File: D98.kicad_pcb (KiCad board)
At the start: 2 copper layers, 40 x 60 mm, 44 parts, among them J1 Conn_01x08, J2 Conn_01x06, J3 Conn_01x06, J4 Conn_01x06, J5 Conn_01x05, J6 Conn_01x04, J7 Conn_01x02, J8 Conn_01x04, U1 YAAJ_BluePill_SWD_Breakout, U2 Poka Yoke

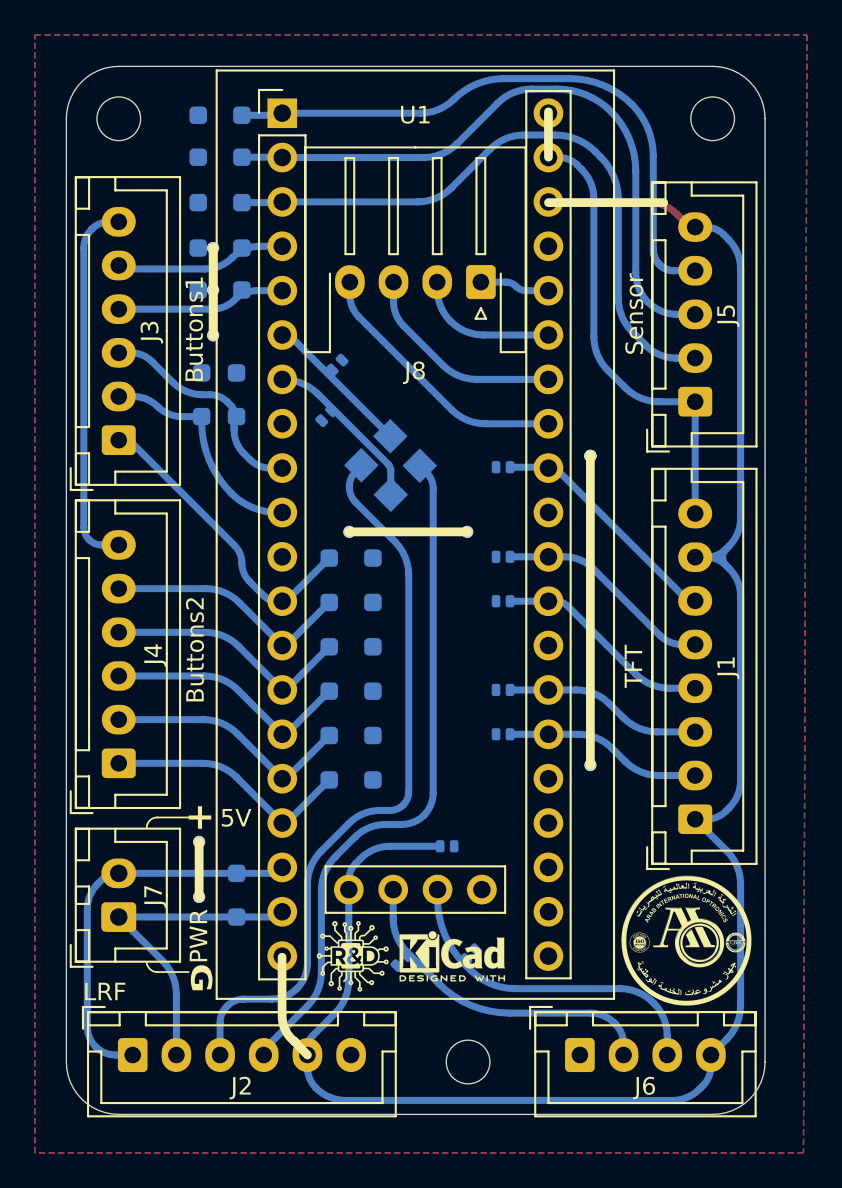
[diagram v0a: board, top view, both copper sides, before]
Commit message: Fix: Changing the EN pin of TFT from always full Brightness to becontrolled Via PWM Pin.
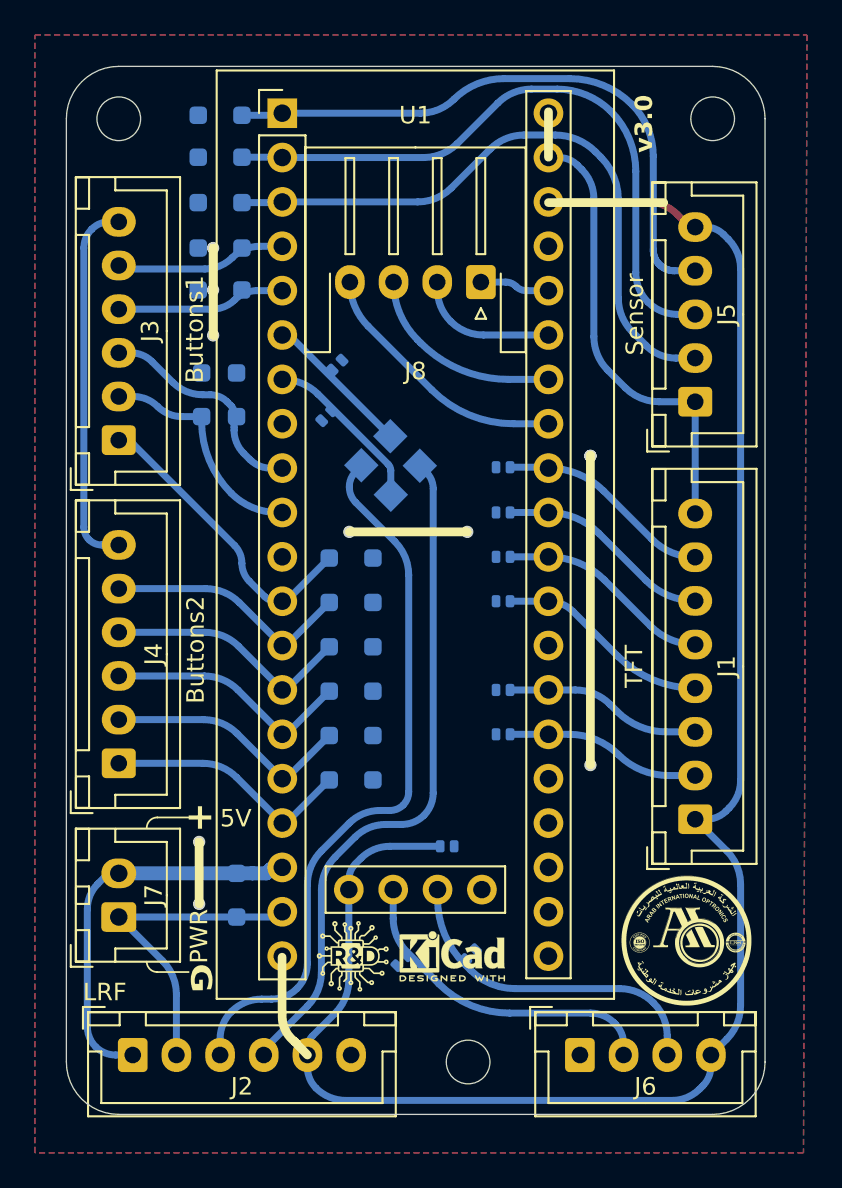
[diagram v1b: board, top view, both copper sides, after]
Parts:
- added D10: LESD8D3.3N3T5G, Diode_SMD:D_SOD-882D, B.Cu at (150.4, 95.9)
- renumbered D10 to D11, D11 to D12, D12 to D13, D13 to D14, D14 to D15, D15 to D16, D16 to D17, D17 to D18, D18 to D19, D19 to D20, D20 to D21, D21 to D22, D22 to D23, D23 to D24, D24 to D25
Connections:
- D25 pad 1: En-3.3v -> 3.3V
- J1 pad 1: En-3.3v -> 3.3V
- J1 pad 6: MOSI-A7 -> En-A6
- J1 pad 7: En-3.3v -> MOSI-A7
- J2 pad 5: En-3.3v -> 3.3V
- J5 pad 5: En-3.3v -> 3.3V
- J6 pad 4: En-3.3v -> 3.3V
- U1 pad 20: En-3.3v -> 3.3V
- U1 pad 31: unconnected-(U1-PA6-Pad31) -> En-A6
- U1 pad 38: En-3.3v -> 3.3V
- U1 pad 44: En-3.3v -> 3.3V
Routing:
- net En-3.3v: track 113.9 -> 0.00 mm
- net 3.3V: track 0.00 -> 110.2 mm
- net En-A6: track 0.00 -> 12.3 mm
- net MOSI-A7: track 13.7 -> 13.0 mm
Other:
- board text added: "${REVISION}"
- board text added: "EN"
- board text added: "EN - A6"

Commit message: fix: changed the EN pin GPIO agian from A6 to A3 because A6 is MSIO.
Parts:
- moved D4 7.62 mm to (150.4, 103.6)
- renumbered D9 to D10, D10 to D4, D4 to D5, D5 to D6, D6 to D7, D7 to D8, D8 to D9
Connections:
- D4 pad 1: En-A6 -> En-A3
- J1 pad 6: En-A6 -> En-A3
- U1 pad 28: unconnected-(U1-PA3-Pad28) -> En-A3
- U1 pad 31: En-A6 -> unconnected-(U1-PA6-Pad31)
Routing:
- net En-A3: track 0.00 -> 20.3 mm
- net En-A6: track 12.3 -> 0.00 mm
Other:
- board text added: "EN - A3"
- board text removed: "EN - A6"

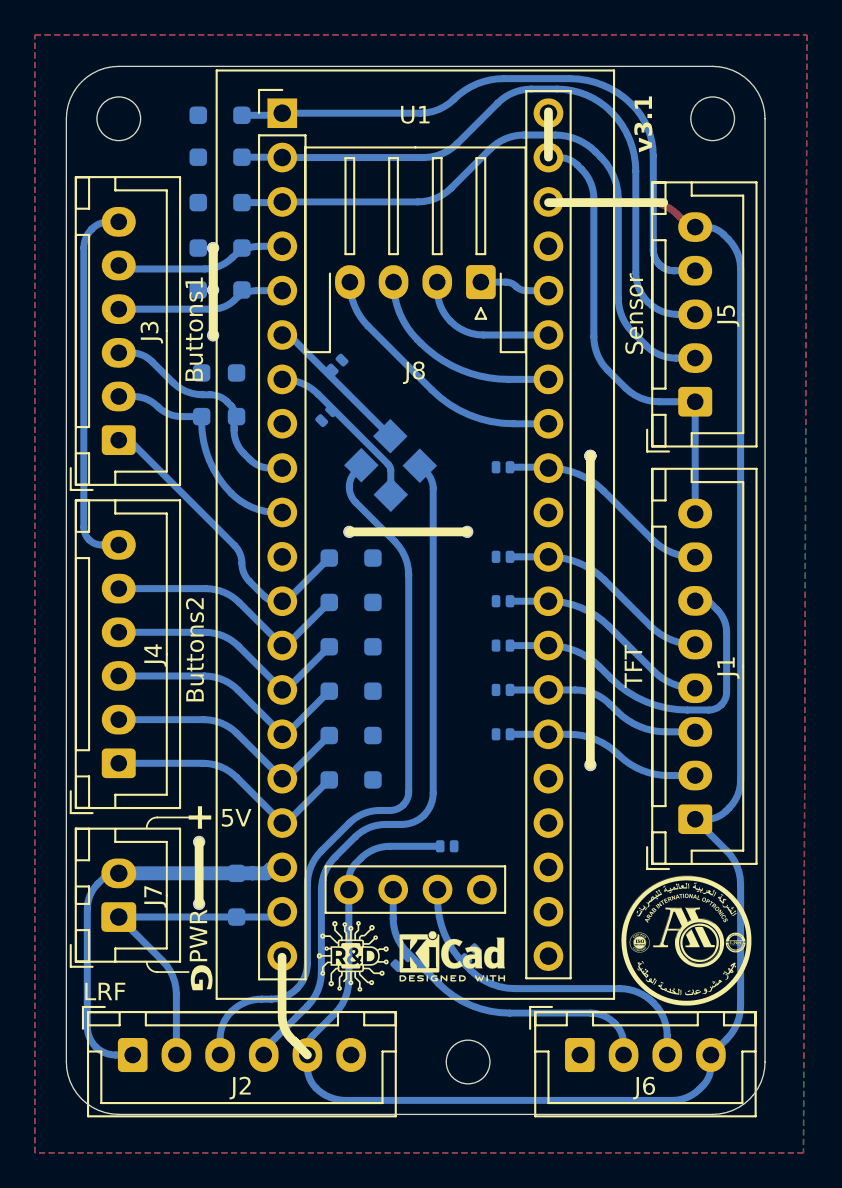
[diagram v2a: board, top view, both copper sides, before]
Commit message: Feat: Change the Rounting of Tracks and the silkscreen.
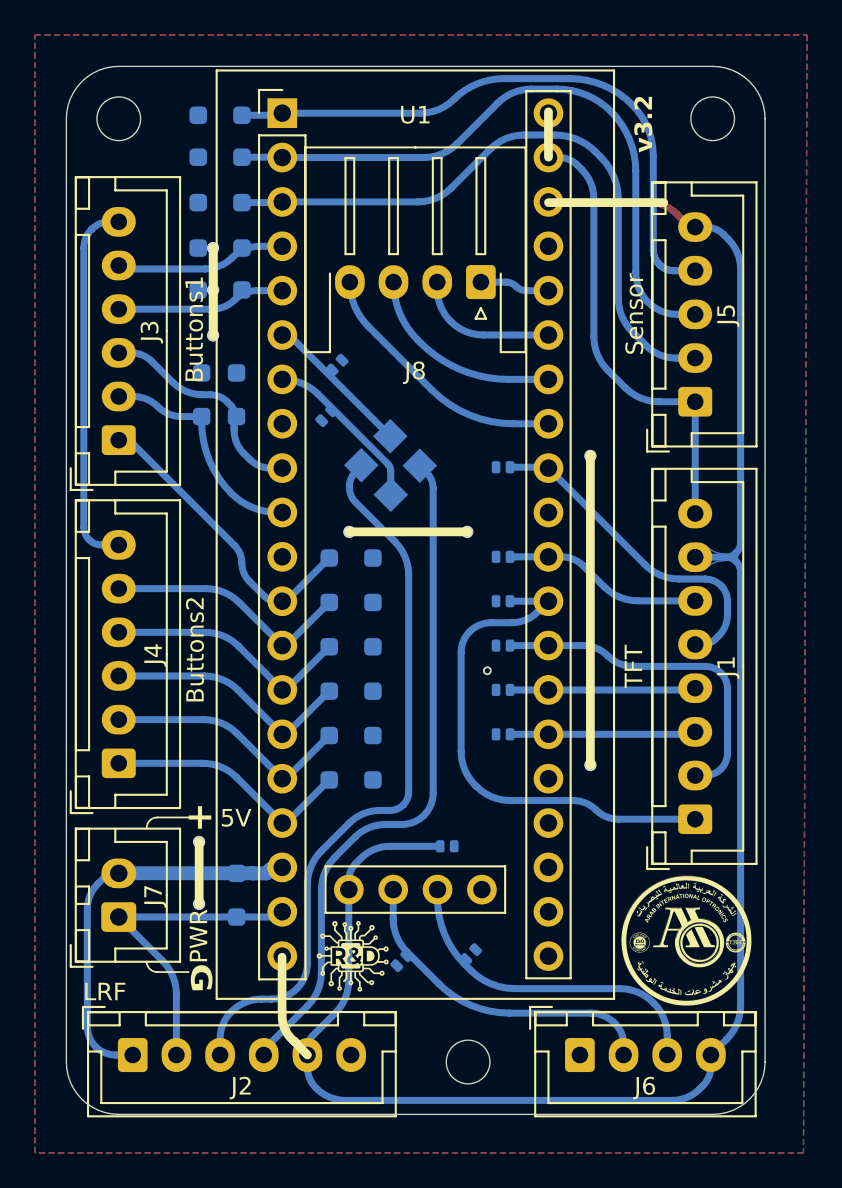
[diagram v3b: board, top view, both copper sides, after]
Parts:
- removed REF** (x2): KiCad-Logo2_5mm_SilkScreen, Symbol:KiCad-Logo2_5mm_SilkScreen
- removed REF**: WEEE-Logo_4.2x6mm_SilkScreen, Symbol:WEEE-Logo_4.2x6mm_SilkScreen
- removed REF**: ESD-Logo_6.6x6mm_SilkScreen, Symbol:ESD-Logo_6.6x6mm_SilkScreen
- added kibuzzard-699AD153: G***, kibuzzard-699AD153, B.Cu at (158.6, 129.2)
- added kibuzzard-699AD186: G***, kibuzzard-699AD186, B.Cu at (135.4, 129.2)
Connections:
- D4 pad 1: En-A3 -> BLK-A3
- J1 pad 1: 3.3V -> CS-A4
- J1 pad 2: DC-A1 -> BLK-A3
- J1 pad 3: RES-A2 -> DC-A1
- J1 pad 4: CS-A4 -> RES-A2
- J1 pad 5: CLK-A5 -> MOSI-A7
- J1 pad 6: En-A3 -> CLK-A5
- J1 pad 7: MOSI-A7 -> 3.3V
- U1 pad 28: En-A3 -> BLK-A3
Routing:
- net En-A3: track 20.3 -> 0.00 mm
- net BLK-A3: track 0.00 -> 19.7 mm
- net CS-A4: track 12.3 -> 29.5 mm
- net MOSI-A7: track 13.0 -> 19.3 mm
- net 3.3V: track 110.2 -> 111.2 mm
- net CLK-A5: track 12.3 -> 11.4 mm
- net RES-A2: track 11.3 -> 10.6 mm
- net DC-A1: track 11.2 -> 10.7 mm
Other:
- board text added: "BLK"
- board text added: "BLK - A3"
- board text removed: "EN"
- board text removed: "EN - A3"
- board text removed: "LRF"
- board text removed: "SWD"
